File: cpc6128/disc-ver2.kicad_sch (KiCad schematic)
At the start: 45 parts, among them IC201 UPD765AC, IC202 SED9420C, IC203 74HC240, IC204 AMS40015, IC205 74LS08, IC206 74LS38, IC207 74LS32, IC208 74LS38, IC209 74LS136, IC210 74LS132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

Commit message: Update title blocks
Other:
- company: (none) -> Amstrad plc
- title: (none) -> CPC6128 MC0020x disk interface
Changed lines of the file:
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@@
 (kicad_sch (version 20211123) (generator eeschema)
   (paper "A3")
+  (title_block
+    (title "CPC6128 MC0020x disk interface")
+    (date "2022-08-20")
+    (rev "1")
+    (company "Amstrad plc")
+  )
   (junction (at 304.165 184.15) (diameter 0) (color 0 0 0 0)
   )

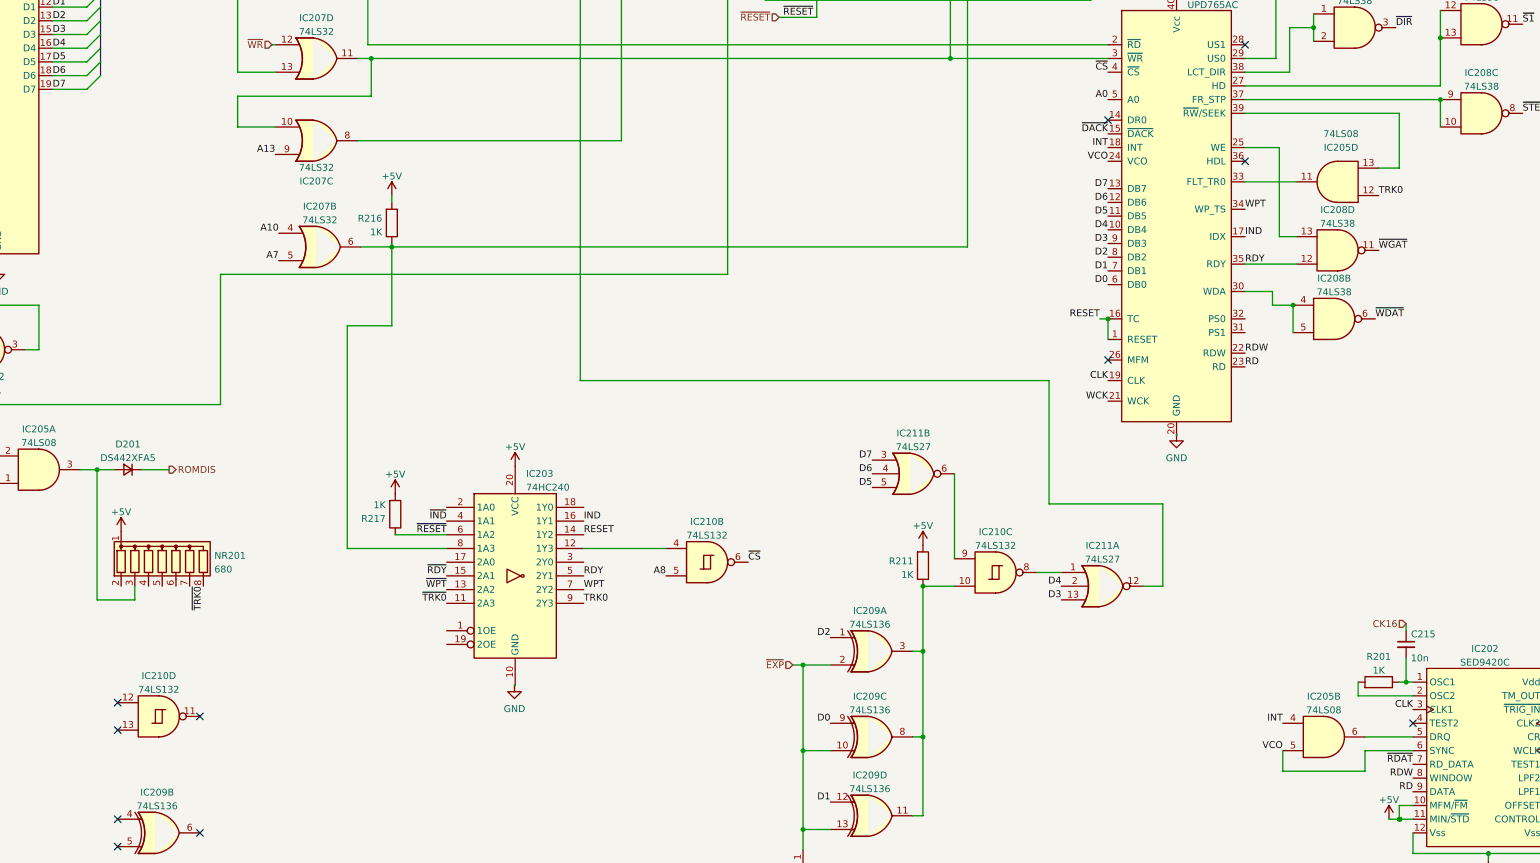
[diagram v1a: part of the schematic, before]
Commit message: Fixes from new top pcb image
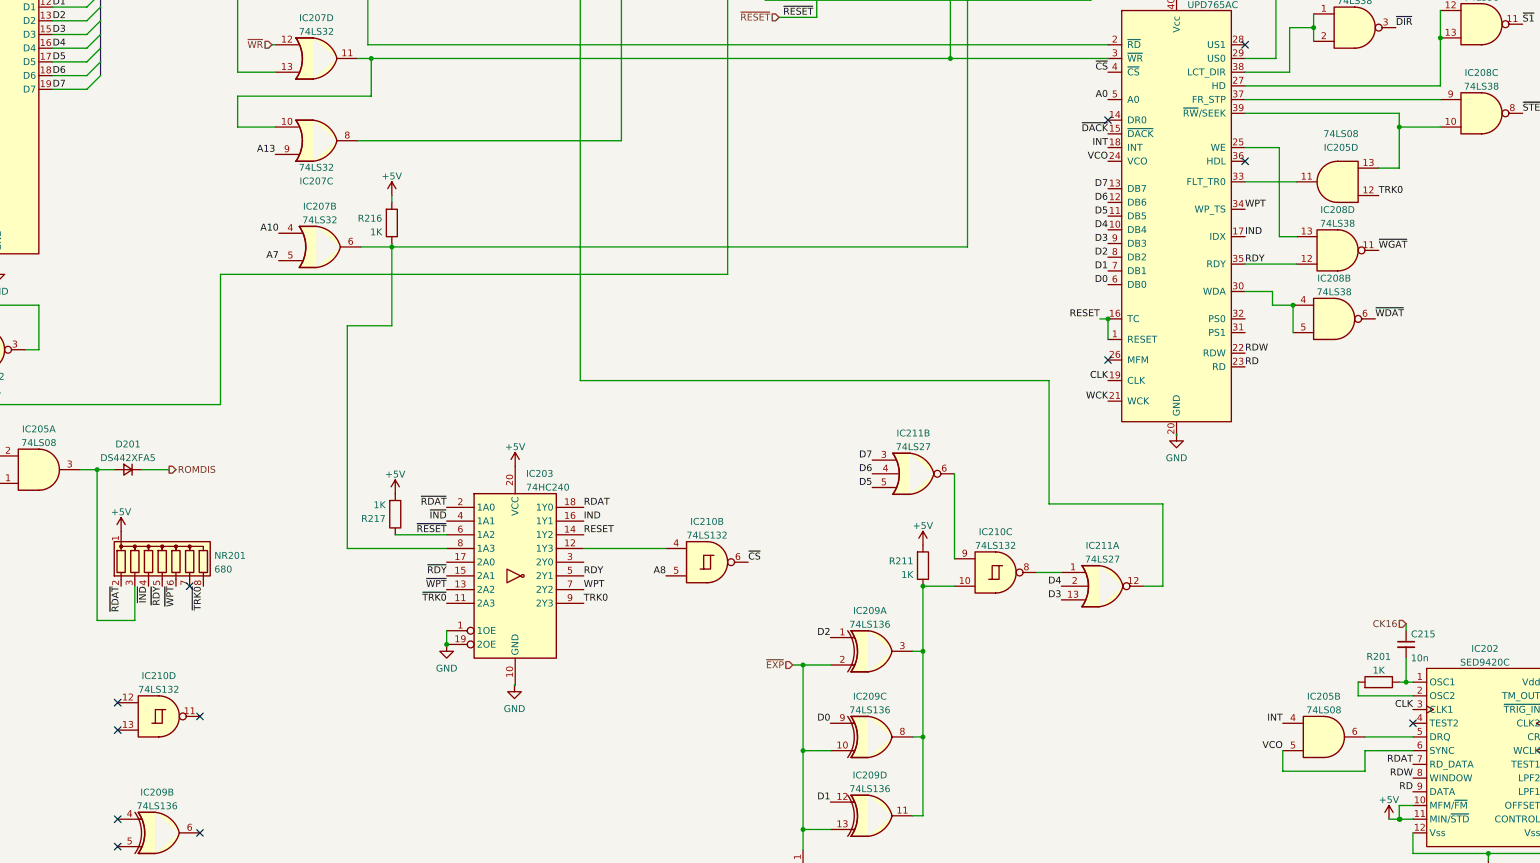
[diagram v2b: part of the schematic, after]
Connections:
- net GND: now also IC203.1 (1OE), IC203.19 (2OE)
- net ~{IND}: now also NR201.4 (R3)
- net ~{RDAT}: now also IC203.2 (1A0), NR201.2 (R1); no longer IC202.7 (RD_DATA)
- net ~{RDY}: now also NR201.5 (R4)
- net ~{WPT}: now also NR201.6 (R5)
- net RDAT: now reaches IC203.18 (1Y0)
- net RDAT: now also IC202.7 (RD_DATA)
- net at IC201.37 (FR_STP), IC208.9: no longer IC208.10
- net at IC201.39 (~{RW}/SEEK), IC205.13: now also IC208.10
- no-connect marks 29 -> 30
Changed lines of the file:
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@@
   (junction (at 389.89 29.845) (diameter 0) (color 0 0 0 0)
   )
-  (junction (at 310.515 76.2) (diameter 0) (color 0 0 0 0)
-  )
   (junction (at 62.865 269.24) (diameter 0) (color 0 0 0 0)
   )
@@
   (junction (at 346.71 69.85) (diameter 0) (color 0 0 0 0)
   )
+  (junction (at 126.365 177.165) (diameter 0) (color 0 0 0 0)
+  )
   (junction (at 31.75 256.54) (diameter 0) (color 0 0 0 0)
   )
@@
   (junction (at 389.89 50.165) (diameter 0) (color 0 0 0 0)
   )
+  (junction (at 302.895 81.28) (diameter 0) (color 0 0 0 0)
+  )
   (junction (at 83.185 269.24) (diameter 0) (color 0 0 0 0)
   )
@@
   (no_connect (at 377.19 57.785))
   (no_connect (at 377.19 60.325))
+  (no_connect (at 78.74 166.37))
   (no_connect (at 332.105 191.77))
   (no_connect (at 332.105 189.23))
@@
     (stroke (width 0) (type default) (color 0 0 0 0))
   )
-  (wire (pts (xy 310.515 76.2) (xy 310.515 81.28))
-    (stroke (width 0) (type default) (color 0 0 0 0))
-  )
   (wire (pts (xy 304.165 173.355) (xy 304.165 174.625))
     (stroke (width 0) (type default) (color 0 0 0 0))
@@
     (stroke (width 0) (type default) (color 0 0 0 0))
   )
-  (wire (pts (xy 68.58 168.91) (xy 61.595 168.91))
+  (wire (pts (xy 68.58 172.72) (xy 61.595 172.72))
     (stroke (width 0) (type default) (color 0 0 0 0))
   )
@@
     (stroke (width 0) (type default) (color 0 0 0 0))
   )
-  (wire (pts (xy 68.58 166.37) (xy 68.58 168.91))
+  (wire (pts (xy 68.58 166.37) (xy 68.58 172.72))
     (stroke (width 0) (type default) (color 0 0 0 0))
   )
@@
     (stroke (width 0) (type default) (color 0 0 0 0))
   )
+  (wire (pts (xy 302.895 81.28) (xy 302.895 78.74))
+    (stroke (width 0) (type default) (color 0 0 0 0))
+  )
   (bus (pts (xy 26.035 61.595) (xy 26.035 64.135))
     (stroke (width 0) (type default) (color 0 0 0 0))
@@
     (stroke (width 0) (type default) (color 0 0 0 0))
   )
-  (wire (pts (xy 302.895 78.74) (xy 302.895 88.9))
-    (stroke (width 0) (type default) (color 0 0 0 0))
-  )
   (wire (pts (xy 213.995 28.575) (xy 213.995 31.75))
     (stroke (width 0) (type default) (color 0 0 0 0))
@@
     (stroke (width 0) (type default) (color 0 0 0 0))
   )
+  (wire (pts (xy 126.365 174.625) (xy 126.365 177.165))
+    (stroke (width 0) (type default) (color 0 0 0 0))
+  )
   (bus (pts (xy 26.035 71.755) (xy 26.035 74.295))
     (stroke (width 0) (type default) (color 0 0 0 0))
@@
     (stroke (width 0) (type default) (color 0 0 0 0))
   )
+  (wire (pts (xy 302.895 81.28) (xy 302.895 88.9))
+    (stroke (width 0) (type default) (color 0 0 0 0))
+  )
   (wire (pts (xy 37.465 256.54) (xy 31.75 256.54))
     (stroke (width 0) (type default) (color 0 0 0 0))
@@
     (stroke (width 0) (type default) (color 0 0 0 0))
   )
+  (wire (pts (xy 302.895 81.28) (xy 310.515 81.28))
+    (stroke (width 0) (type default) (color 0 0 0 0))
+  )
   (wire (pts (xy 364.49 201.93) (xy 364.49 204.47))
     (stroke (width 0) (type default) (color 0 0 0 0))
@@
     (stroke (width 0) (type default) (color 0 0 0 0))
   )
-  (wire (pts (xy 61.595 168.91) (xy 61.595 144.78))
+  (wire (pts (xy 61.595 172.72) (xy 61.595 144.78))
     (stroke (width 0) (type default) (color 0 0 0 0))
   )
@@
     (effects (font (size 1.27 1.27)) (justify right bottom))
   )
+  (label "~{RDAT}" (at 66.04 166.37 270)
+    (effects (font (size 1.27 1.27)) (justify right bottom))
+  )
   (label "D0" (at 197.485 191.77 180)
     (effects (font (size 1.27 1.27)) (justify right bottom))
@@
     (effects (font (size 1.27 1.27)) (justify left bottom))
   )
+  (label "RDAT" (at 151.765 151.765 0)
+    (effects (font (size 1.27 1.27)) (justify left bottom))
+  )
   (label "~{RDAT}" (at 377.19 121.285 180)
     (effects (font (size 1.27 1.27)) (justify right bottom))
@@
     (effects (font (size 1.27 1.27)) (justify left bottom))
   )
+  (label "~{WPT}" (at 76.2 166.37 270)
+    (effects (font (size 1.27 1.27)) (justify right bottom))
+  )
   (label "WCK" (at 332.105 196.85 0)
     (effects (font (size 1.27 1.27)) (justify left bottom))
   )
+  (label "~{RDY}" (at 73.66 166.37 270)
+    (effects (font (size 1.27 1.27)) (justify right bottom))
+  )
   (label "~{WPT}" (at 126.365 167.005 180)
     (effects (font (size 1.27 1.27)) (justify right bottom))
@@
     (effects (font (size 1.27 1.27)) (justify right bottom))
   )
+  (label "~{IND}" (at 71.12 166.37 270)
+    (effects (font (size 1.27 1.27)) (justify right bottom))
+  )
   (label "A8" (at 167.005 164.465 180)
     (effects (font (size 1.27 1.27)) (justify right bottom))
@@
     (effects (font (size 1.27 1.27)) (justify right bottom))
   )
-  (label "~{RDAT}" (at 305.435 199.39 180)
+  (label "RDAT" (at 305.435 199.39 180)
     (effects (font (size 1.27 1.27)) (justify right bottom))
   )
@@
     (effects (font (size 1.27 1.27)) (justify right bottom))
   )
+  (label "~{RDAT}" (at 126.365 151.765 180)
+    (effects (font (size 1.27 1.27)) (justify right bottom))
+  )
   (label "D1" (at 53.34 59.055 0)
     (effects (font (size 1.27 1.27)) (justify left bottom))
@@
     (pin "9")
   )
+  (symbol (lib_id "power:GND") (at 126.365 177.165 0) (unit 1)
+    (in_bom yes) (on_board yes) (fields_autoplaced)
+    (property "Reference" "#PWR0235" (id 0) (at 126.365 183.515 0)
+      (effects (font (size 1.27 1.27)) hide)
+    )
+    (property "Value" "GND" (id 1) (at 126.365 181.6084 0))
+    (property "Footprint" "" (id 2) (at 126.365 177.165 0)
+      (effects (font (size 1.27 1.27)) hide)
+    )
+    (property "Datasheet" "" (id 3) (at 126.365 177.165 0)
+      (effects (font (size 1.27 1.27)) hide)
+    )
+    (pin "1")
+  )
   (symbol (lib_id "Device:C_Small") (at 52.705 262.89 180) (unit 1)

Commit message: Minor cleanups
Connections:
- net ~{WR}: no longer IC207.12
- no-connect marks 30 -> 32
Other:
- moved on the sheet: C218, IC203, IC207B, IC207C, IC208A, IC209A, IC209C, IC209D, IC210B, IC210C, IC211A, IC211B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

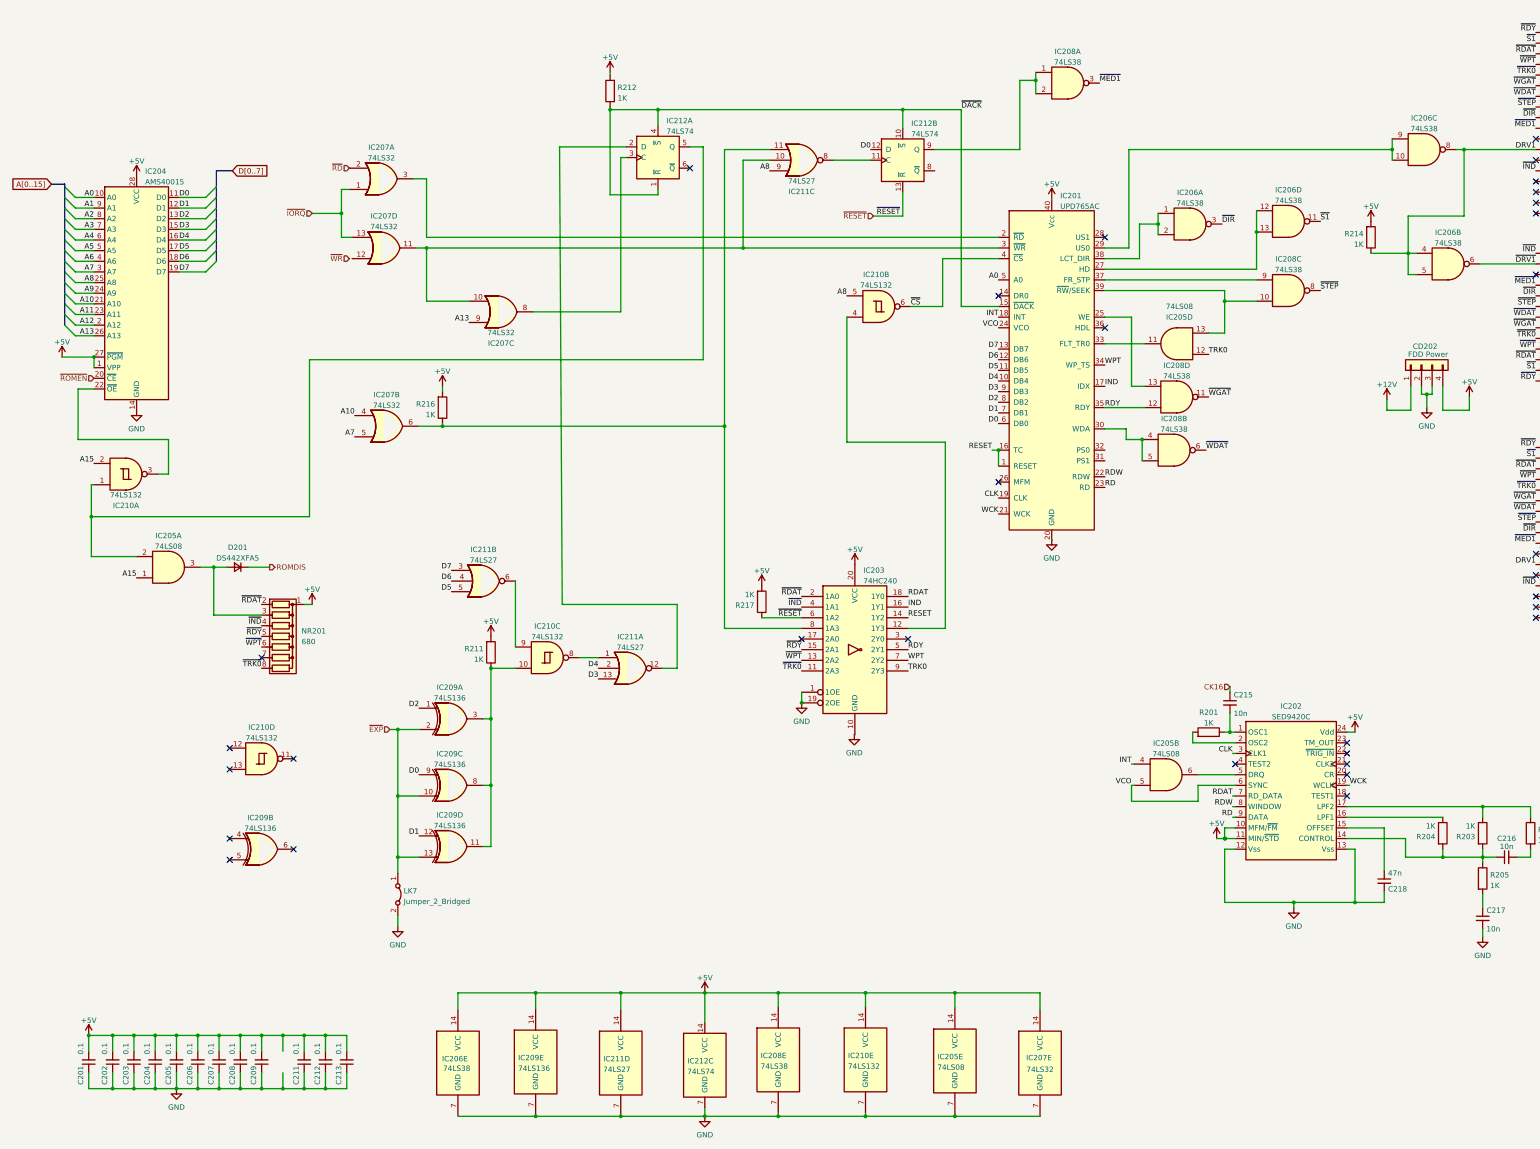
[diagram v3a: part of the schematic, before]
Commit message: Correct C136 (missing) and C314 (wrong footprint) Thanks @orzel!
Also migrated to KiCad 9.
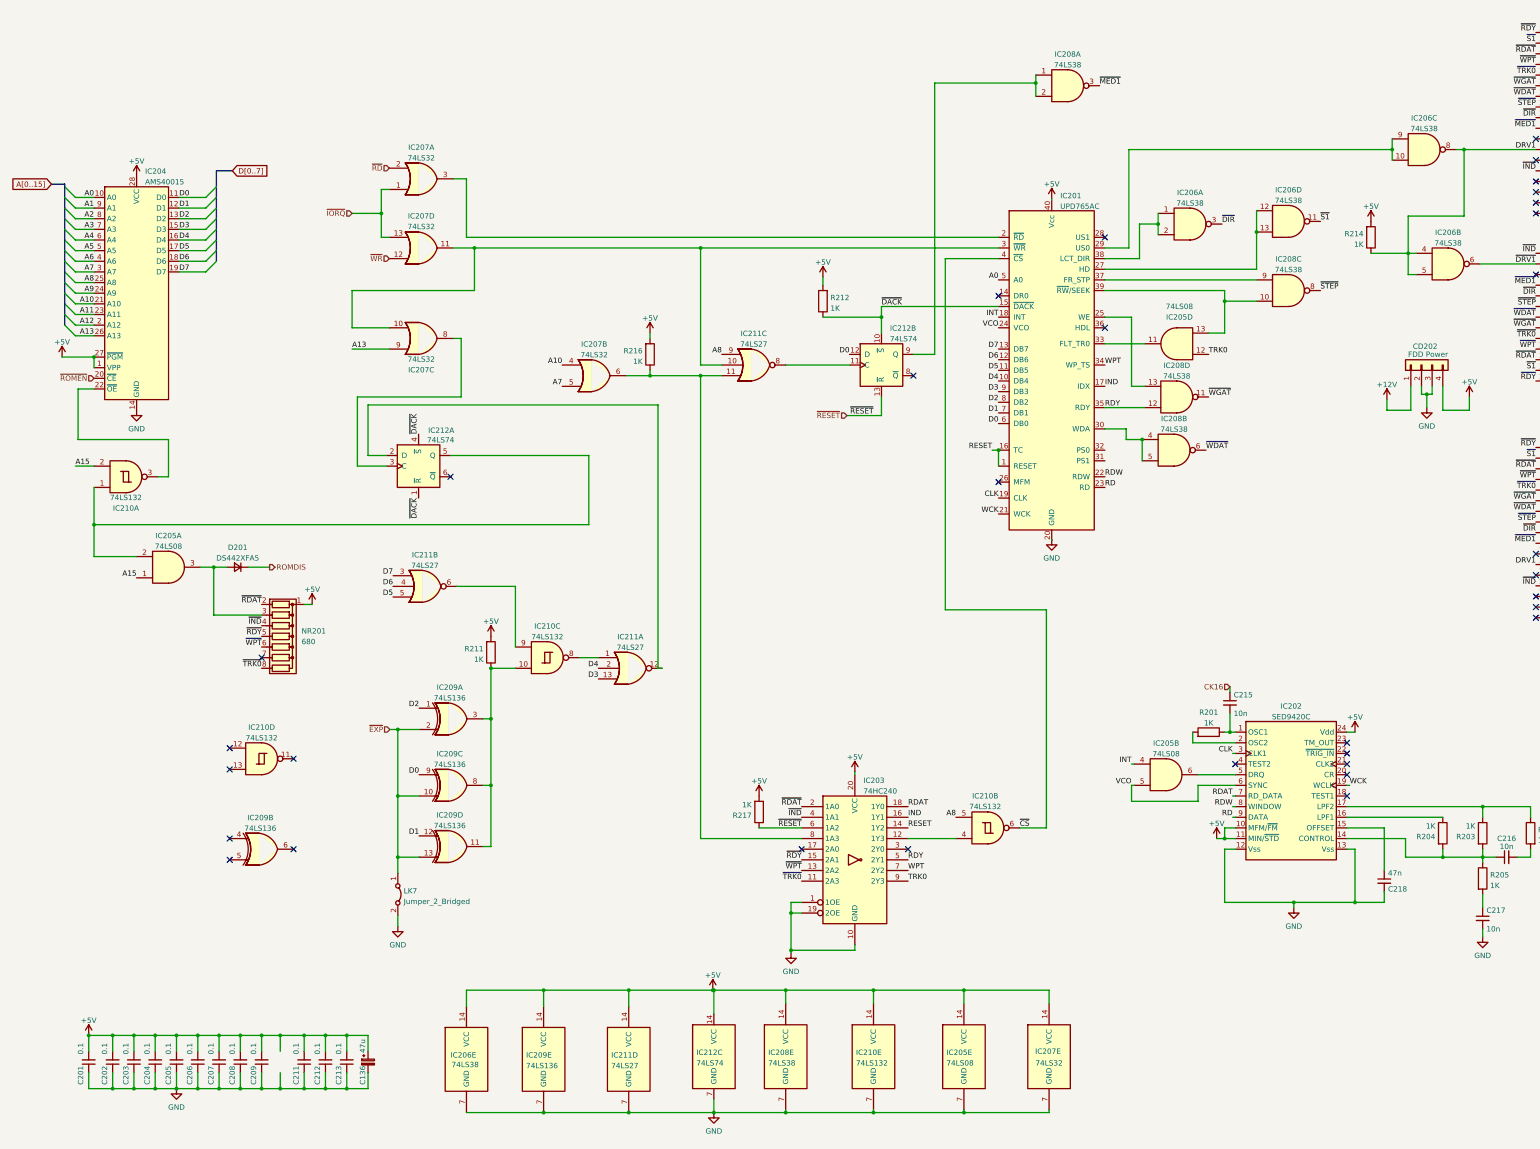
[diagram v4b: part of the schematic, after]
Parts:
- added C136: 47u, Amstrad-CPC:CP_Radial_D4.0mm_P5.00mm, symbol Device:C_Polarized_Small
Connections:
- net +5V: now also C136.1
- net GND: now also C136.2
- net ~{WR}: now also IC207.12
- no-connect marks 32 -> 33
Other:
- moved on the sheet: IC203, IC205E, IC206E, IC207A, IC207B, IC207C, IC207D, IC207E, IC208A, IC208E, IC209E, IC210A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
